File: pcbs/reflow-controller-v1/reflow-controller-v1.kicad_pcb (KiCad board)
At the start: 4 copper layers, 85.2 x 238.5 mm, 154 parts, among them J1 PinHeader 1x03 P2.54mm, J101 EB163A-03-C-180, J102 EB163A-02-C-180, J103 EB163A-02-C-180, J104 EB163A-02-C-180, J105 EB163A-02-C-180, J106 PinHeader 1x03 P2.54mm, J1101 EB163A-04-C-180, J1201 EB163A-04-C-180, J1301 EB163A-04-C-180, J201 PinHeader 1x02 P2.54mm, J3 SWD, J4 UART, M101 47053-1000, Q1601 MMBT3904, Q1602 140357145200, Q201 PMV65XP, SW1001 TS04-66-85-BK-160-SMT, SW1002 PEC12R-3220F-S0024, SW1003 TS04-66-85-BK-160-SMT, U1 TMP1075DSG, U1101 MAX31865ATP+, U1201 MAX31865ATP+, U1301 MAX31865ATP+, U2 TMP1075DSG, U201 TPS62933DRLR, U202 AZ1117-3.3, U3 STM32G474VETx, U301 MOC3043SM, U401 MOC3043SM, U501 MOC3043SM, U601 MOC3043SM

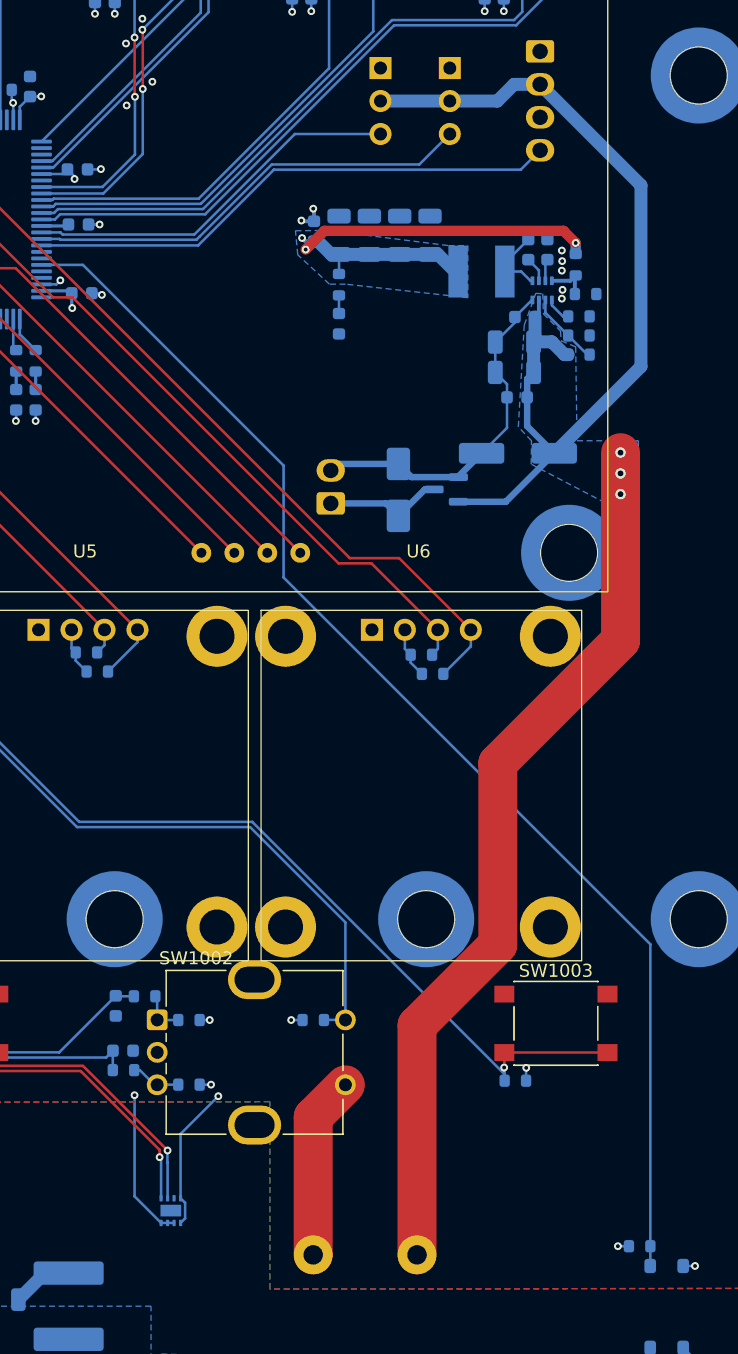
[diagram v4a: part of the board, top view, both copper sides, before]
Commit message: move misplaced 5V output caps
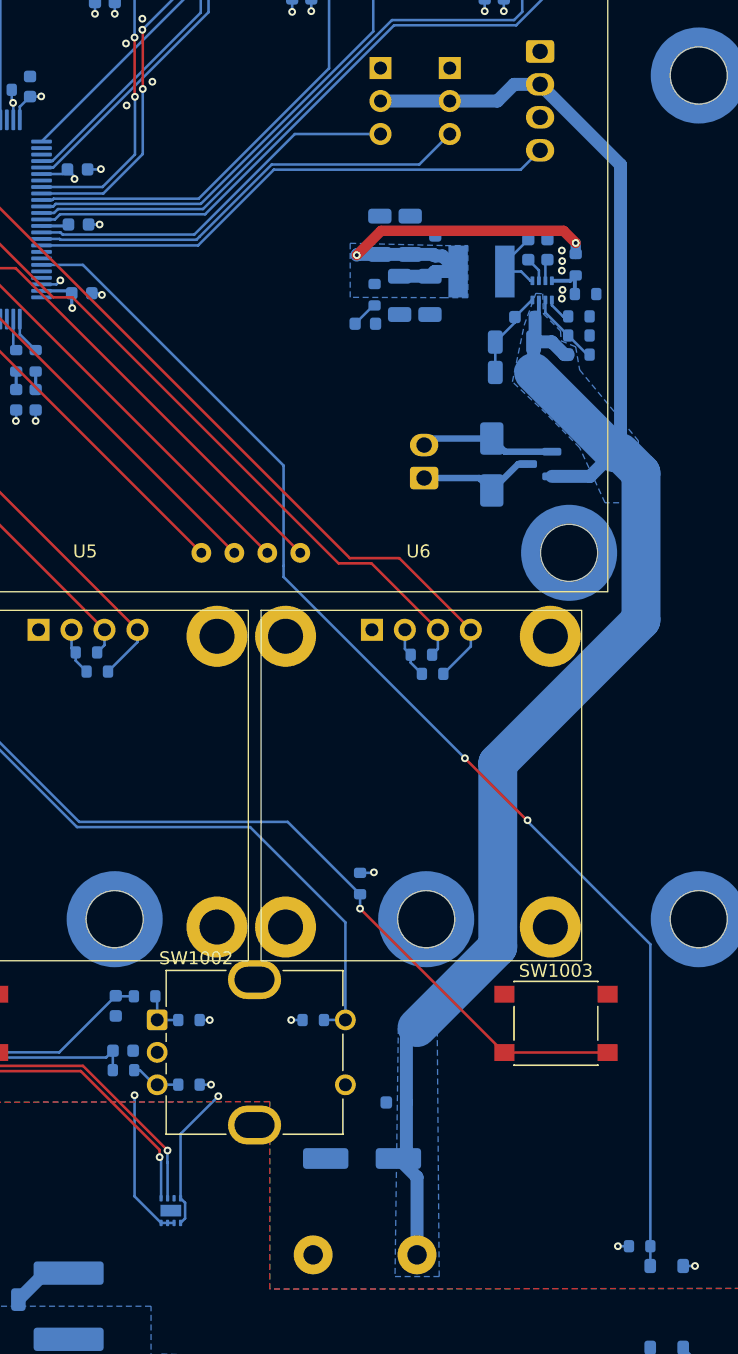
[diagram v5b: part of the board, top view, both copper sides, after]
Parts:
- moved C202 55.6 mm to (71.6, 149.7)
- moved C201 55.1 mm to (74.3, 145.3)
- moved R1009 19.3 mm to (71.5, 128.5), turned to -90 degrees
- moved C212 9.41 mm to (77.3, 79.3)
- moved D202 7.46 mm to (81.6, 96.2)
- moved J201 7.46 mm to (76.4, 97.2)
- moved Q201 7.46 mm to (85.3, 96.2)
- moved C211 6.57 mm to (74.5, 83.2), turned to -90 degrees
- moved C208 4.63 mm to (76.9, 83.2), turned to -90 degrees
- moved R205 2.85 mm to (72.6, 83.1)
- moved D201 2.03 mm to (71.9, 85.3), turned to 180 degrees
- moved C210 0.81 mm to (73.0, 78.5)
- moved C209 0.81 mm to (75.3, 78.5)
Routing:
- net GND: track 79.5 -> 53.4 mm, vias 53 -> 51
- net +3V3: track 110.2 -> 104.1 mm, vias 33 -> 32
- net /Buttons/SW_2: track 97.9 -> 95.1 mm
- net +5V: track 140.6 -> 138.2 mm, vias 3 -> 0
- net /AC DC Converter/LED: track 1.40 -> 2.08 mm
- net /Zero Crossing detector/Crossing: track 98.4 -> 98.5 mm, vias 0 -> 2

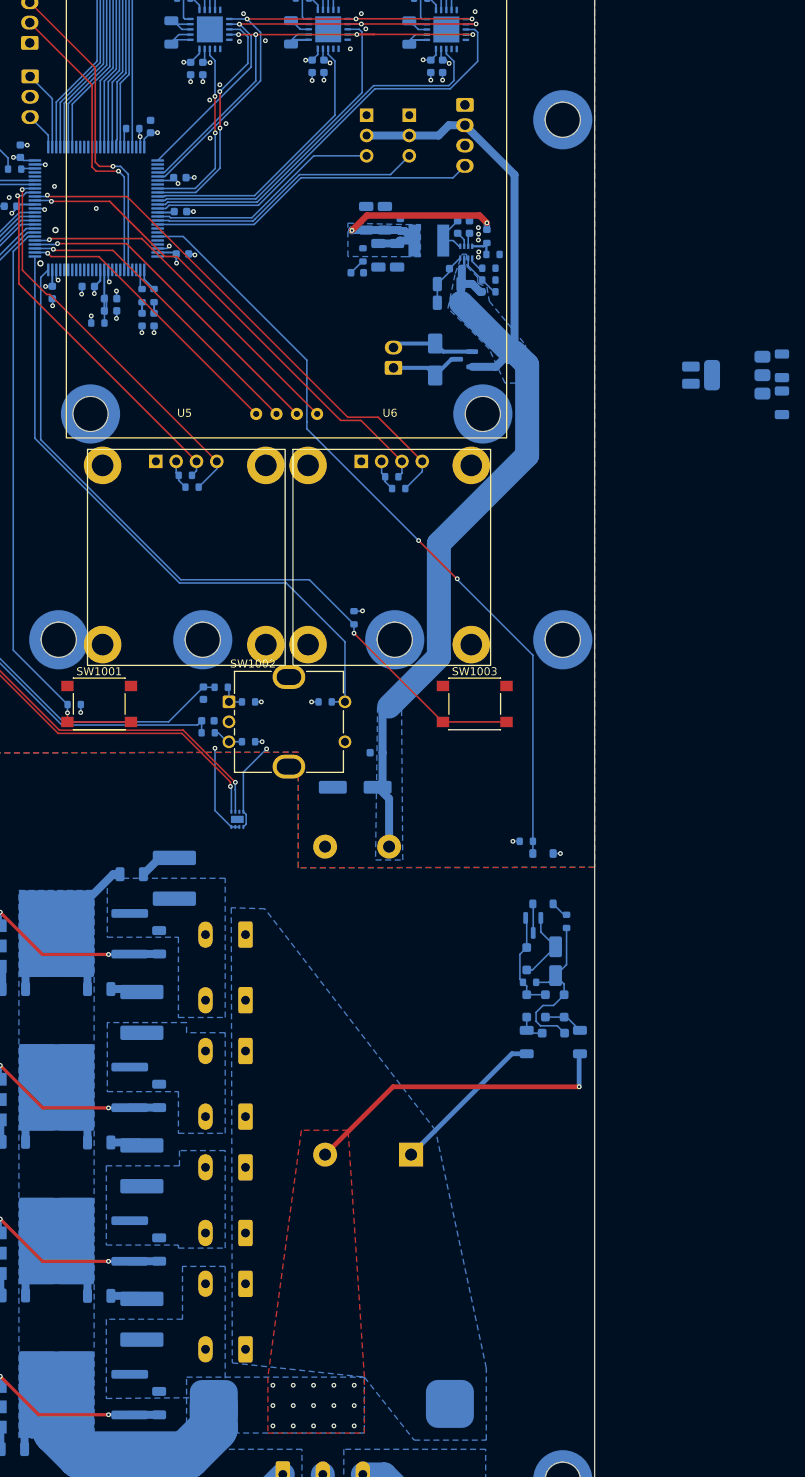
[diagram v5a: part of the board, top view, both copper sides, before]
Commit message: update analog voltage ldo placement&routing
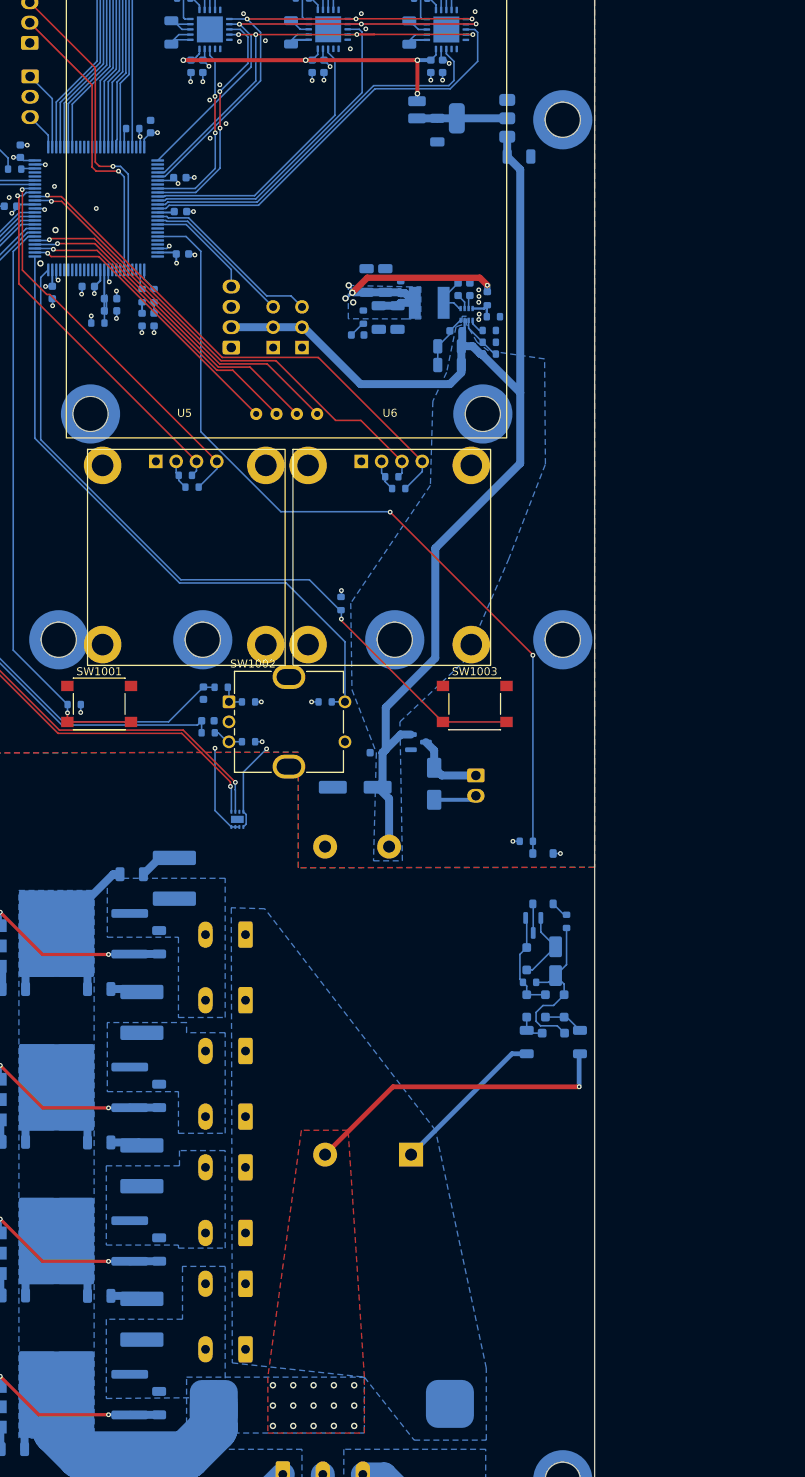
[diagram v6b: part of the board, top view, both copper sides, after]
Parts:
- moved D202 53.0 mm to (81.5, 149.2), turned to 90 degrees
- moved C214 52.2 mm to (81.9, 67.5), turned to -90 degrees
- moved J201 52.0 mm to (86.7, 148.2), turned to -90 degrees
- moved Q201 48.2 mm to (79.5, 144.0), turned to 0 degrees
- moved FB201 47.7 mm to (79.3, 65.0), turned to -90 degrees
- moved U202 45.3 mm to (87.5, 66.0)
- moved C213 45.0 mm to (92.1, 70.8), turned to 0 degrees
- moved M101 42.1 mm to (56.1, 94.7), turned to 90 degrees
- moved J1 33.7 mm to (61.4, 94.7), turned to 0 degrees
- moved J106 30.1 mm to (65.0, 94.7), turned to 0 degrees
- moved C205 7.78 mm to (84.2, 92.6)
- moved C209 7.78 mm to (75.4, 86.3)
- moved C210 7.78 mm to (73.1, 86.3)
- moved C212 7.78 mm to (77.3, 87.1)
- moved D201 7.78 mm to (71.9, 93.1)
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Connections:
- C214 pad 2: GNDA -> GND
- R1102 pad 2: GNDA -> GND
- R1201 pad 2: GNDA -> GND
- R1301 pad 2: GNDA -> GND
- U1101 pad 10: GNDA -> GND
- U1101 pad 16: GNDA -> GND
- U1101 pad 21: GNDA -> GND
- U1201 pad 10: GNDA -> GND
- U1201 pad 16: GNDA -> GND
- U1201 pad 21: GNDA -> GND
- U1301 pad 10: GNDA -> GND
- U1301 pad 16: GNDA -> GND
- U1301 pad 21: GNDA -> GND
- U202 pad 1: GNDA -> GND
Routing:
- net +3.3VA: track 0.00 -> 43.2 mm, vias 0 -> 4
- net /Fan_PWM: track 41.4 -> 13.7 mm
- net /Servo2: track 34.9 -> 18.9 mm
- net +5V: track 138.2 -> 150.7 mm
- net Net-(U202-VO): track 0.00 -> 11.3 mm
- net /Zero Crossing detector/Crossing: track 98.5 -> 106.6 mm
- net /Servo1: track 29.4 -> 22.7 mm
- net +3V3: track 104.1 -> 98.0 mm
- net GND: track 53.4 -> 48.7 mm
